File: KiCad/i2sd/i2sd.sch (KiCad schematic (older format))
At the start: 22 parts, among them IC1 ATMEGA8-AI, P1 CONN_4, P2 CONN_4, P3 CONN_4, SW1 SW_PUSH, X1 CRYSTAL

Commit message: 2011-05-11 : i2sd schematic revision
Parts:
- removed R4, R6, R8: 2k2, symbol R
- added R1: 10k, symbol R
- added U1: MCP_1700, symbol MCP_1700
- R2: value 2k2 -> 10k
- R3: renamed from R5; value 1k -> 10k
- R4: renamed from R3; value 1k -> 10k
- R5: renamed from R7; value 1k -> 10k
- R6: renamed from R1; value 1k -> 10k
- renumbered C2 to C1, C1 to C2, R11 to R7, R9 to R8, R10 to R9
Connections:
- net SD_DATA_IN is gone; now on net MOSI: R4.2, SD1.2 (DATA_IN/CMD)
- net +5V: now also R2.1, R3.1, R4.1, R6.1, SD1.4 (VCC), R1.1, U1.2 (VOUT), U1.3 (VIN)
- net GND: now also U1.1 (GND); no longer R2.2
- net MISO: now also R5.2
- net MOSI: no longer R4.1
- net SCK: now also R6.2, SD1.5 (CLK); no longer R6.1
- net SCL: now also R1.2
- net SDA: now also R2.2
- net SD_CS: now also IC1.14 (PB2(SS/OC1B))
- removed net 3V3: R5.2, SD1.4 (VCC)
- removed net SD_CLK: R2.1, R6.2, SD1.5 (CLK)
- removed net SS: IC1.14 (PB2(SS/OC1B)), R3.1
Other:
- note removed: "why do we need two of these ?"
- moved on the sheet: R3, R4, R5, R6

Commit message: 2011-05-12 : i2sd : Schematic and PCB
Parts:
- removed R5: 10k, symbol R
- added C5, C6: 100u, CP_5x11mm, symbol C_POL
- added C7: 100n, C2, symbol C
- added P4, P5, P6, P7: CONN_4, pin_strip_4, symbol CONN_4
- added P8: FTDI, pin_strip_6-90, symbol CONN_6
- added U2: 74LS125, SO14E, symbol 74LS125
- C1, C2: footprint (none) -> C2
- C3, C4: footprint (none) -> C1
- P1: value CONN_4 -> WP_CD; footprint (none) -> pin_strip_4
- P2: value CONN_4 -> COMM_R; footprint (none) -> pin_strip_4
- P3: value CONN_4 -> COMM_L; footprint (none) -> pin_strip_4
- R1, R2, R3, R4, R6, R7, R8, R9: footprint (none) -> R1
- SD1: footprint (none) -> Memory_Card_SD_3M
- SW1: footprint (none) -> SW-PB
- U1: footprint (none) -> SOT23-5
- X1: footprint (none) -> XTAL
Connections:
- net +5V: now also C6.1; no longer R3.1, R4.1, R6.1, R8.1, R9.1, SD1.4 (VCC), U1.2 (VOUT)
- net GND: now also C5.2, C6.2, P8.1, P8.2, U2.1 (E), U2.10 (E), U2.4 (E), U2.7 (GND), U2.7 (GND), U2.7 (GND), U2.7 (GND); no longer SD1.11 (GND), SD1.12 (GND)
- net MOSI: now also U2.6 (O); no longer SD1.2 (DATA_IN/CMD)
- net SCK: now also U2.3 (O); no longer SD1.5 (CLK)
- net SD_CS: now also U2.9 (D); no longer IC1.14 (PB2(SS/OC1B)), R3.2
- net B_02: now reaches IC1.1 (PD3(INT1))
- net B_02: now also P4.2 (P2)
- net B_15: now reaches IC1.10 (PD6(AIN0))
- net B_15: now also P7.3 (P3)
- net B_14: now reaches IC1.11 (PD7(AIN1))
- net B_14: now also P7.2 (P2)
- net B_13: now reaches IC1.12 (PB0(ICP))
- net B_13: now also P7.1 (P1)
- net B_12: now reaches IC1.13 (PB1(OC1A))
- net B_12: now also P6.4 (P4)
- net B_11: now reaches IC1.19 (ADC6)
- net B_11: now also P6.3 (P3)
- net B_01: now reaches IC1.2 (PD4(XCK/T0))
- net B_01: now also P4.1 (P1)
- net B_10: now reaches IC1.22 (ADC7)
- net B_10: now also P6.2 (P2)
- net B_09: now reaches IC1.23 (PC0(ADC0))
- net B_09: now also P6.1 (P1)
- net B_08: now reaches IC1.24 (PC1(ADC1))
- net B_08: now also P5.4 (P4)
- net B_07: now reaches IC1.25 (PC2(ADC2))
- net B_07: now also P5.3 (P3)
- net B_06: now reaches IC1.26 (PC3(ADC3))
- net B_06: now also P5.2 (P2)
- net RESET: now reaches IC1.29 (PC6(/RESET)), R7.2, SW1.2
- net RESET: now also C7.2
- net RXD: now reaches IC1.30 (PD0(RXD))
- net RXD: now also P8.4
- net TXD: now reaches IC1.31 (PD1(TXD))
- net TXD: now also P8.5
- net B_03: now reaches IC1.32 (PD2(INT0))
- net B_03: now also P4.3 (P3)
- net B_16: now reaches IC1.9 (PD5(T1))
- net B_16: now also P7.4 (P4)
- new net: C7.1, P8.6
- new net SD_CLK: SD1.5 (CLK), U2.2 (D)
- new net SD_DATA_IN: SD1.2 (DATA_IN/CMD), U2.5 (D)
- new net SS: IC1.14 (PB2(SS/OC1B)), R3.2, U2.8 (O)
- new net VCC: C5.1, R3.1, R4.1, R6.1, R8.1, R9.1, SD1.4 (VCC), U1.2 (VOUT), U2.12 (D), U2.13 (E), U2.14 (VCC), U2.14 (VCC), U2.14 (VCC), U2.14 (VCC)
- no-connect marks 18 -> 10
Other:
- note added: "I/O Breakout"
- moved on the sheet: C1, C2, C3, C4, IC1, P2, P3, R1, R2, R3, R4, R6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

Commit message: 2011-05-12 i2sd PCB updates
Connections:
- net GND: now also SD1.11 (GND), SD1.12 (GND)
- no-connect marks 10 -> 8

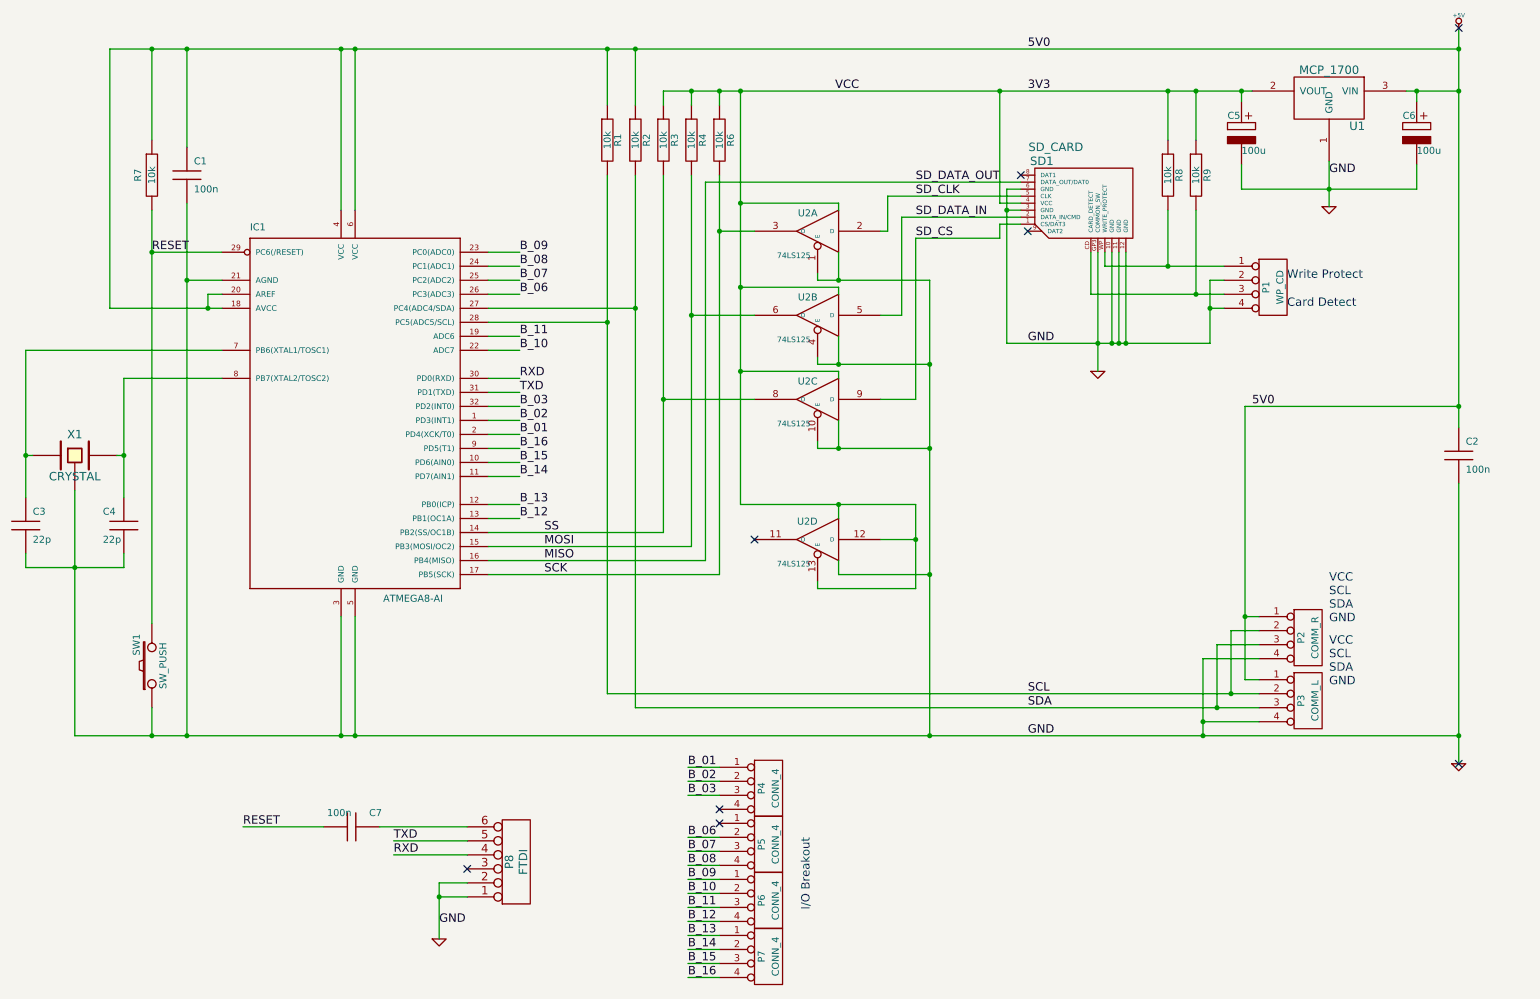
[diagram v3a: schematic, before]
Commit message: 2011-05-13 i2sd revised PCB layout
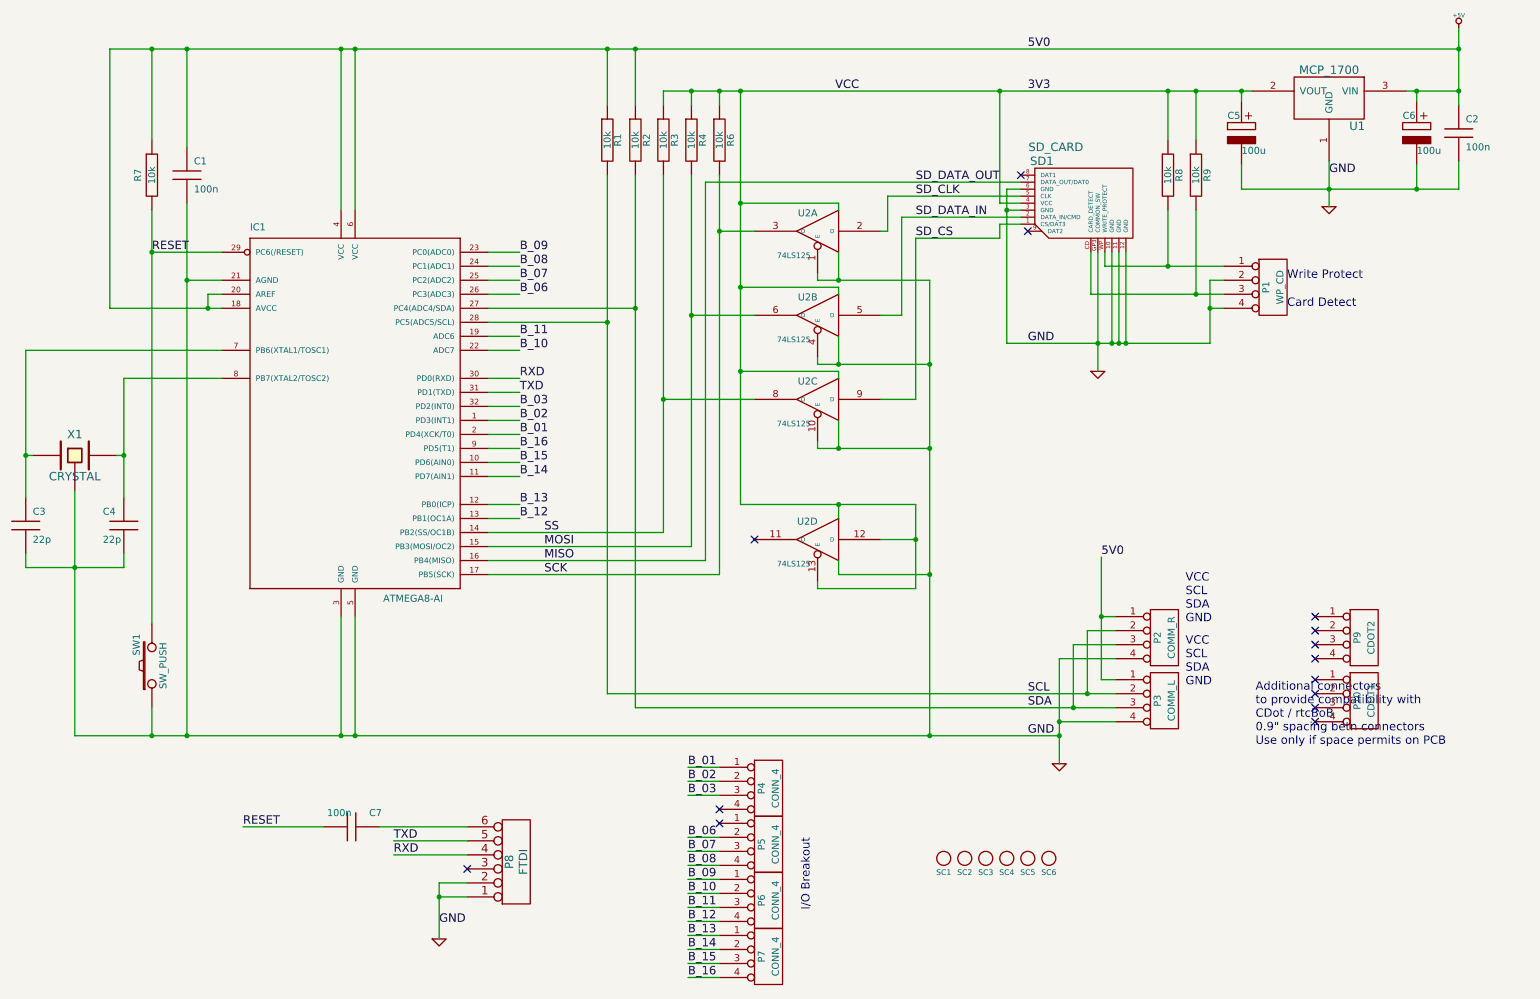
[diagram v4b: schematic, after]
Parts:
- added P10: CDOT1, pin_strip_4, symbol CONN_4
- added P9: CDOT2, pin_strip_4, symbol CONN_4
- added SC1, SC2, SC3, SC4, SC5, SC6: SCREW, vite_3mm, symbol SCREW
- SD1: footprint Memory_Card_SD_3M -> Memory_Card_SD_Tyco
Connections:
- no-connect marks 8 -> 14
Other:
- note added: "Additional connectors\nto provide compatibility with\nCDot / rtcBoB\n0.9" spacing betn connectors\nUse only if space permits on PCB"
- moved on the sheet: C2, P2, P3

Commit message: 2011-05-13 i2sd board and schematic updates
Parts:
- removed P10: CDOT1, pin_strip_4, symbol CONN_4
- removed P4, P5, P6, P7: CONN_4, pin_strip_4, symbol CONN_4
- removed P9: CDOT2, pin_strip_4, symbol CONN_4
- removed SC4: SCREW, vite_3mm, symbol SCREW
- added B1, B10, B11, B12, B13, B14, B2, B3, B4, B5, B6, B7, B8, B9: I/O, symbol I/O
- added P4, P5, P6, P7: CONN_I/O, symbol CONN_I/O
- added P9: ISP, symbol ISP
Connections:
- net B_15 is gone; now on net B_13: IC1.10 (PD6(AIN0))
- net B_16 is gone; now on net B_14: IC1.9 (PD5(T1))
- net +5V: now also P9.2
- net B_01: now also B1.1
- net B_02: now also B2.1
- net B_03: now also B3.1
- net B_06: now also IC1.24 (PC1(ADC1)), B6.1; no longer IC1.26 (PC3(ADC3))
- net B_07: now also IC1.23 (PC0(ADC0)), B7.1; no longer IC1.25 (PC2(ADC2))
- net B_08: now also IC1.22 (ADC7), B8.1; no longer IC1.24 (PC1(ADC1))
- net B_09: now also IC1.19 (ADC6), B9.1; no longer IC1.23 (PC0(ADC0))
- net B_10: now also IC1.13 (PB1(OC1A)), B10.1; no longer IC1.22 (ADC7)
- net B_11: now also IC1.12 (PB0(ICP)), B11.1; no longer IC1.19 (ADC6)
- net B_12: now also IC1.11 (PD7(AIN1)), B12.1; no longer IC1.13 (PB1(OC1A))
- net B_13: now also B13.1; no longer IC1.12 (PB0(ICP))
- net B_14: now also B14.1; no longer IC1.11 (PD7(AIN1))
- net GND: now also P9.6
- net MISO: now also P9.1
- net MOSI: now also P9.4
- net RESET: now also P9.5
- net SCK: now also P9.3
- new net B_04: B4.1, IC1.26 (PC3(ADC3))
- new net B_05: B5.1, IC1.25 (PC2(ADC2))
- no-connect marks 14 -> 20
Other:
- note removed: "Additional connectors\nto provide compatibility with\nCDot / rtcBoB\n0.9" spacing betn connectors\nUse only if space permits on PCB"
- moved on the sheet: C7

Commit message: 2011-05-14 i2sd PCB and SCH almost final - need to check
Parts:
- B1, B10, B11, B12, B13, B14, B2, B3, B4, B5, B6, B7, B8, B9: footprint (none) -> I/O
- P1: footprint pin_strip_4 -> WP_CD
- P4, P5, P6, P7: footprint (none) -> CONN_I/O
- P9: footprint (none) -> ISP
- U1: footprint SOT23-5 -> SOT23-3
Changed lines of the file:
@@
-EESchema Schematic File Version 2  date 05/13/11 18:11:31
+EESchema Schematic File Version 2  date 05/14/11 17:46:40
 LIBS:i2sd
 LIBS:power
@@
 F 0 "B14" H 4405 3650 40  0000 L CNN
 F 1 "I/O" H 4325 3705 30  0001 C CNN
+F 2 "I/O" H 4325 3650 60  0001 C CNN
 	1    4325 3650
 	1    0    0    -1
@@
 F 0 "B13" H 4405 3750 40  0000 L CNN
 F 1 "I/O" H 4325 3805 30  0001 C CNN
+F 2 "I/O" H 4325 3750 60  0001 C CNN
 	1    4325 3750
 	1    0    0    -1
@@
 F 0 "B12" H 4405 3850 40  0000 L CNN
 F 1 "I/O" H 4325 3905 30  0001 C CNN
+F 2 "I/O" H 4325 3850 60  0001 C CNN
 	1    4325 3850
 	1    0    0    -1
@@
 F 0 "B11" H 4405 4050 40  0000 L CNN
 F 1 "I/O" H 4325 4105 30  0001 C CNN
+F 2 "I/O" H 4325 4050 60  0001 C CNN
 	1    4325 4050
 	1    0    0    -1
@@
 F 0 "B10" H 4405 4150 40  0000 L CNN
 F 1 "I/O" H 4325 4205 30  0001 C CNN
+F 2 "I/O" H 4325 4150 60  0001 C CNN
 	1    4325 4150
 	1    0    0    -1
@@
 F 0 "B9" H 4405 2850 40  0000 L CNN
 F 1 "I/O" H 4325 2905 30  0001 C CNN
+F 2 "I/O" H 4325 2850 60  0001 C CNN
 	1    4325 2850
 	1    0    0    -1
@@
 F 0 "B8" H 4405 2950 40  0000 L CNN
 F 1 "I/O" H 4325 3005 30  0001 C CNN
+F 2 "I/O" H 4325 2950 60  0001 C CNN
 	1    4325 2950
 	1    0    0    -1
@@
 F 0 "B7" H 4405 2250 40  0000 L CNN
 F 1 "I/O" H 4325 2305 30  0001 C CNN
+F 2 "I/O" H 4325 2250 60  0001 C CNN
 	1    4325 2250
 	1    0    0    -1
@@
 F 0 "B6" H 4405 2350 40  0000 L CNN
 F 1 "I/O" H 4325 2405 30  0001 C CNN
+F 2 "I/O" H 4325 2350 60  0001 C CNN
 	1    4325 2350
 	1    0    0    -1
@@
 F 0 "B5" H 4405 2450 40  0000 L CNN
 F 1 "I/O" H 4325 2505 30  0001 C CNN
+F 2 "I/O" H 4325 2450 60  0001 C CNN
 	1    4325 2450
 	1    0    0    -1
@@
 F 0 "B4" H 4405 2550 40  0000 L CNN
 F 1 "I/O" H 4325 2605 30  0001 C CNN
+F 2 "I/O" H 4325 2550 60  0001 C CNN
 	1    4325 2550
 	1    0    0    -1
@@
 F 0 "B3" H 4405 3350 40  0000 L CNN
 F 1 "I/O" H 4325 3405 30  0001 C CNN
+F 2 "I/O" H 4325 3350 60  0001 C CNN
 	1    4325 3350
 	1    0    0    -1
@@
 F 0 "B2" H 4405 3450 40  0000 L CNN
 F 1 "I/O" H 4325 3505 30  0001 C CNN
+F 2 "I/O" H 4325 3450 60  0001 C CNN
 	1    4325 3450
 	1    0    0    -1
@@
 F 0 "B1" H 4405 3550 40  0000 L CNN
 F 1 "I/O" H 4325 3605 30  0001 C CNN
+F 2 "I/O" H 4325 3550 60  0001 C CNN
 	1    4325 3550
 	1    0    0    -1
@@
 F 0 "P7" V 5900 7275 50  0000 C CNN
 F 1 "CONN_I/O" V 6000 7275 50  0000 C CNN
+F 2 "CONN_I/O" H 5950 7275 60  0001 C CNN
 	1    5950 7275
 	1    0    0    -1
@@
 F 0 "P6" V 5900 6875 50  0000 C CNN
 F 1 "CONN_I/O" V 6000 6875 50  0000 C CNN
+F 2 "CONN_I/O" H 5950 6875 60  0001 C CNN
 	1    5950 6875
 	1    0    0    -1
@@
 F 0 "P5" V 5900 6475 50  0000 C CNN
 F 1 "CONN_I/O" V 6000 6475 50  0000 C CNN
+F 2 "CONN_I/O" H 5950 6475 60  0001 C CNN
 	1    5950 6475
 	1    0    0    -1
@@
 F 0 "P4" V 5900 6075 50  0000 C CNN
 F 1 "CONN_I/O" V 6000 6075 50  0000 C CNN
+F 2 "CONN_I/O" H 5950 6075 60  0001 C CNN
 	1    5950 6075
 	1    0    0    -1
@@
 F 0 "P9" V 1950 6600 60  0000 C CNN
 F 1 "ISP" V 2050 6600 60  0000 C CNN
+F 2 "ISP" H 2000 6600 60  0001 C CNN
 	1    2000 6600
 	1    0    0    -1
@@
 F 0 "U1" H 9750 1050 60  0000 C CNN
 F 1 "MCP_1700" H 9950 1450 60  0000 C CNN
-F 2 "SOT23-5" H 9950 1200 60  0001 C CNN
+F 2 "SOT23-3" H 9950 1200 60  0001 C CNN
 	1    9950 1200
 	-1   0    0    -1
@@
 F 0 "P1" V 9500 2500 50  0000 C CNN
 F 1 "WP_CD" V 9600 2500 50  0000 C CNN
-F 2 "pin_strip_4" H 9550 2500 60  0001 C CNN
+F 2 "WP_CD" H 9550 2500 60  0001 C CNN
 	1    9550 2500
 	1    0    0    -1

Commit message: 2011-05-19 i2sd pcb changes (smd)
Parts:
- removed C3, C4: 22p, C1, symbol C
- removed P1: WP_CD, WP_CD, symbol CONN_4
- removed R9: 10k, R1, symbol R
- removed SC3, SC5, SC6: SCREW, vite_3mm, symbol SCREW
- added D1, D2: LED, symbol LED
- added R5: 470E, symbol R
- R8: value 10k -> 470E; footprint R1 -> (none)
- SW1: footprint SW-PB -> pin_strip_2
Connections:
- net B_02: now also R5.1
- net B_03: now also R8.1
- net GND: now also D1.2 (K), D2.2 (K)
- net MOSI: now also U2.5 (D); no longer U2.6 (O)
- net SCK: now also U2.2 (D); no longer U2.3 (O)
- net SD_CLK: now also U2.3 (O); no longer U2.2 (D)
- net SD_CS: now also U2.8 (O); no longer U2.9 (D)
- net SD_DATA_IN: now also U2.6 (O); no longer U2.5 (D)
- net SS: now also U2.9 (D); no longer U2.8 (O)
- net VCC: no longer R8.1
- net at SD1.WP (WRITE_PROTECT): no longer R8.2
- new net: D1.1 (A), R5.2
- new net: D2.1 (A), R8.2
- no-connect marks 20 -> 22
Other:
- note removed: "Card Detect"
- note removed: "Write Protect"
- moved on the sheet: P4, P5, P6, P7

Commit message: 2011-05-21 : i2sd : PCB / SCH / Gerbers Final
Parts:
- added P10, P11: CD2, Sck-04-F-SMT, symbol CONN_4
- added P12, P13: CD1, Sck-04-F-SMT, symbol CONN_4
- C1, C2, C7: footprint C2 -> c_0805
- D1, D2: footprint (none) -> d_0805
- P4, P5, P6, P7: footprint CONN_I/O -> pin_strip_4
- R1, R2, R3, R4, R6, R7: footprint R1 -> r_0805
- R5, R8: footprint (none) -> r_0805
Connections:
- net +5V: now also P10.3 (P3), P11.3 (P3)
- net GND: now also P10.4 (P4), P11.4 (P4)
- net SCL: now also P10.2 (P2), P11.2 (P2)
- net SDA: now also P10.1 (P1), P11.1 (P1)
- no-connect marks 22 -> 30
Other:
- note added: "Additional SMD headers for mounting\non rtcBoB/ChronoDot pins"
- note added: "Mounting Holes"
